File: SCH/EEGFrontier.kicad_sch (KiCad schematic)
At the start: 29 parts, among them J1 Conn_01x08_Pin, SW1 SW_Push, U1 102010428, U2 ADS1299-4PAGR

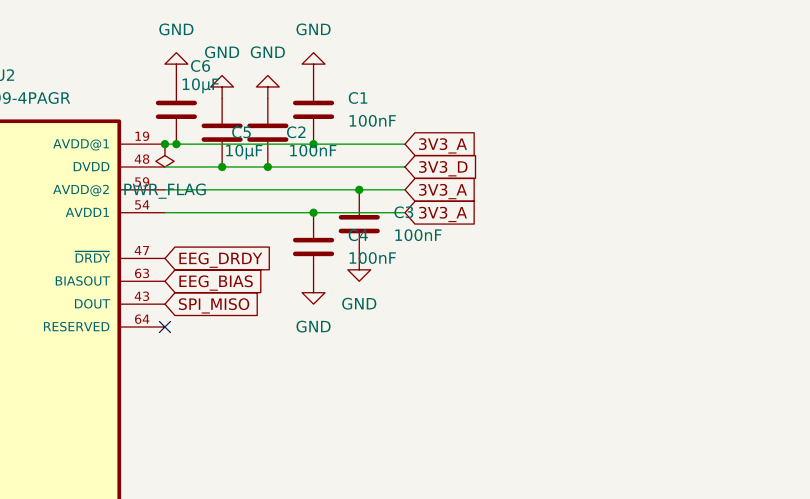
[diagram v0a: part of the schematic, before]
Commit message: Critical: Fixed float 3V3 #5
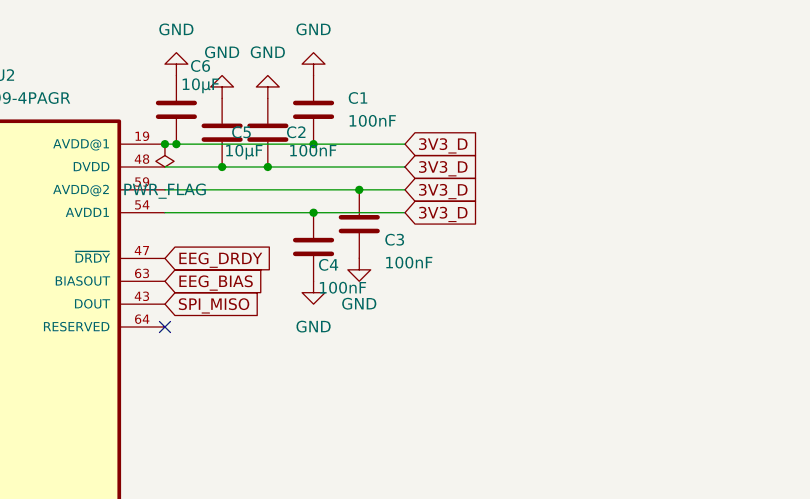
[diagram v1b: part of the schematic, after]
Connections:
- net DVDD is gone; now on net AVDD@1: C2.1, C5.1, R1.1, R3.1, U1.12 (3V3), U2.48 (DVDD), U2.50 (DVDD)
